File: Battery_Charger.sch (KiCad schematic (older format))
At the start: 40 parts, among them J1 OpenVent_Barrel_Connector, Q10 2N7002BK, Q11 2N7002BK, Q12 2N7002BK, Q8 PBSS5350Z, U13 TLV7042DGKR, U14 BQ24450DW, U16 TLV2333IDR

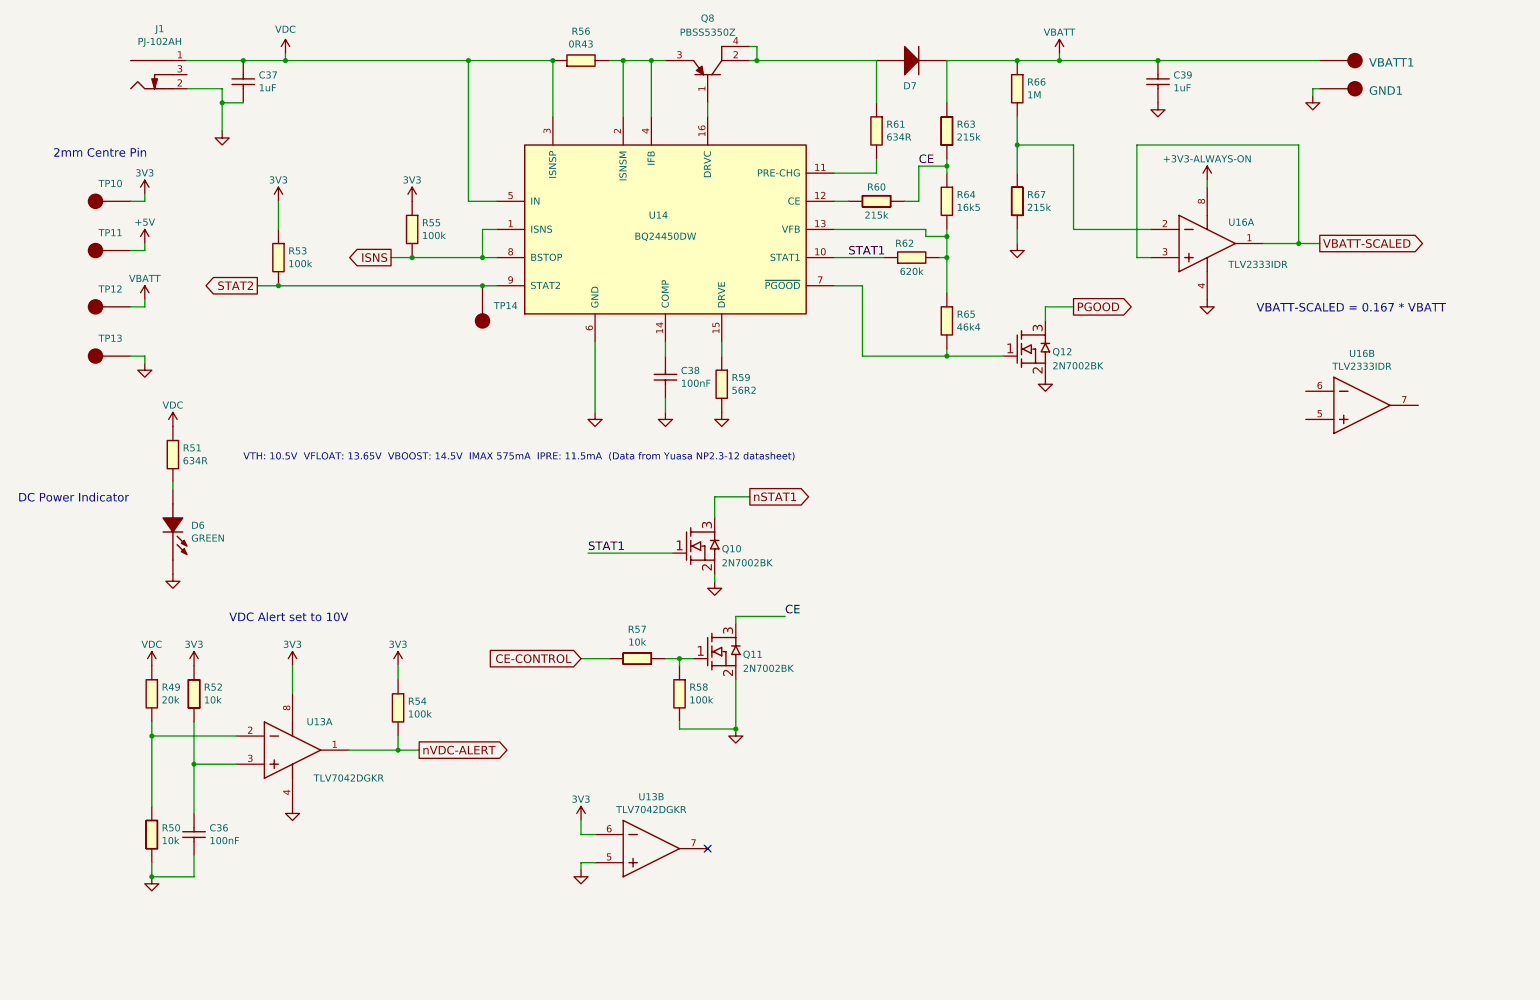
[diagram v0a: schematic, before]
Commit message: Still had some text cleanups to do plus fixed a couple of minor circuit issues.
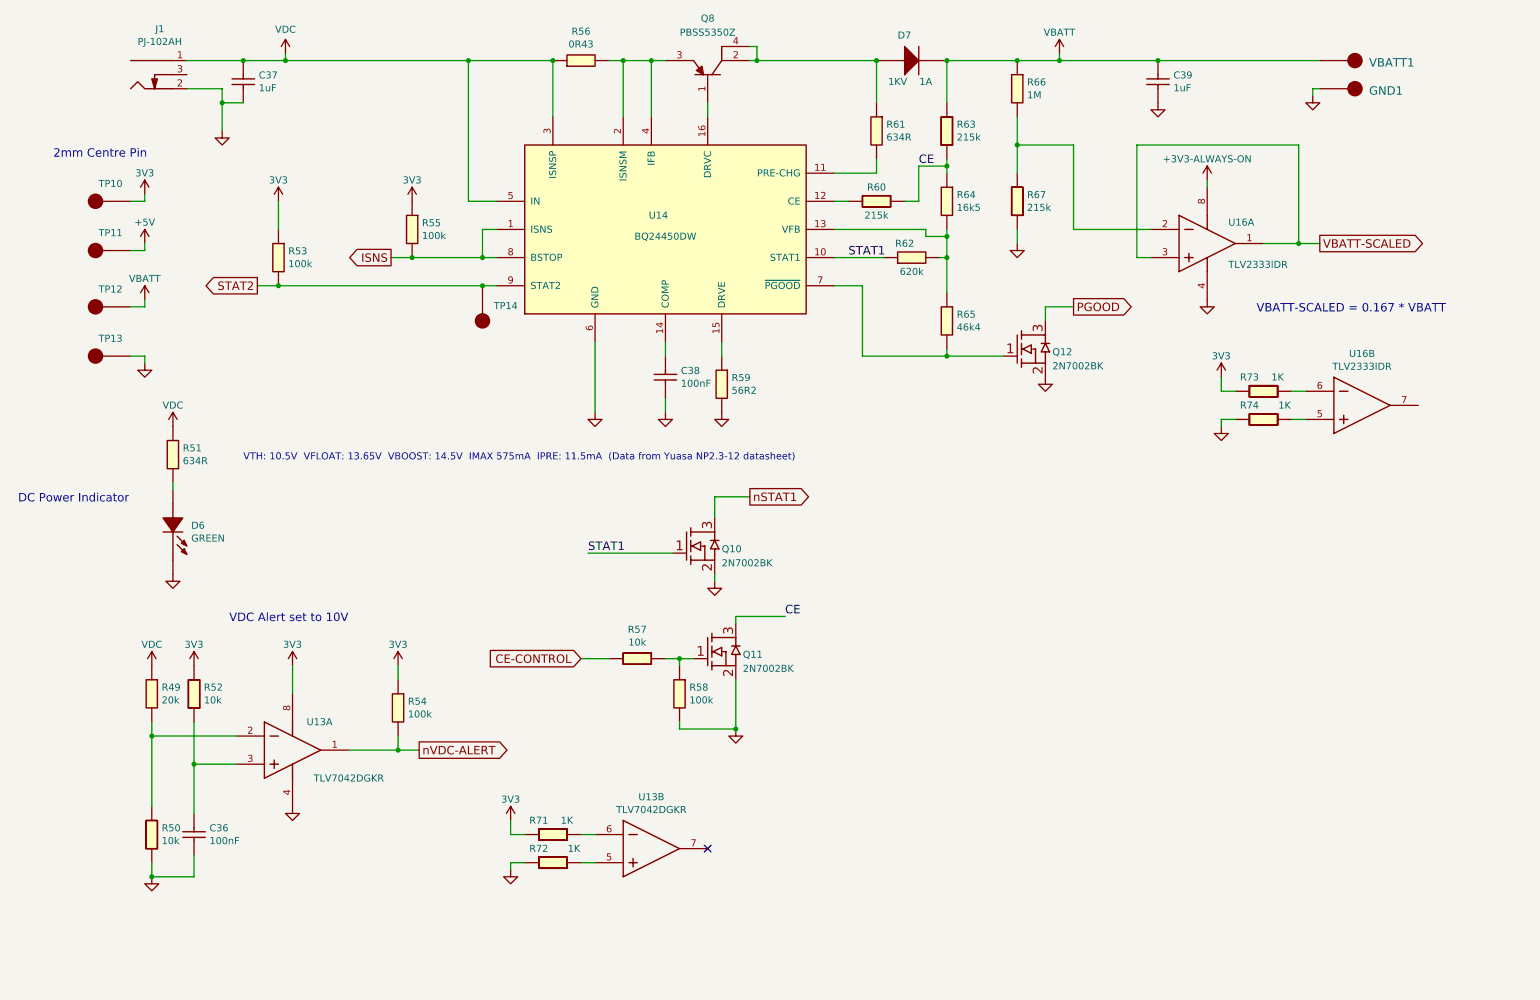
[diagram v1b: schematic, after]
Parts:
- added R71, R72, R73, R74: 1K_0603_Chip_Resistor,_1%,_0.1W, symbol OpenVent:1K_0603_Chip_Resistor,_1%,_0.1W
- D7: value ~ -> DIODE_GEN_PURP_1KV_1A_SMA; Current (none) -> 1A; ManufacturerPN S1M-13-F -> (none); Mfr_PN (none) -> S1M-13-F; Voltage (none) -> 1KV
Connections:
- net +3V3: now also R71.1, R73.1; no longer U13.6 (INB-)
- net GND: now also R72.1, R74.1; no longer U13.5 (INB+)
- net at U16.5 (INB+): now also R74.2
- net at U16.6 (INB-): now also R73.2
- new net: R71.2, U13.6 (INB-)
- new net: R72.2, U13.5 (INB+)
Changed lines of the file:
@@
 L OpenVent:GND #GND_047
 U 1 1 5F8DD1BD
-P 4550 6800
-F 0 "#GND_047" H 4550 6800 20  0001 C CNN
-F 1 "GND" H 4550 6730 30  0001 C CNN
-F 2 "" H 4550 6800 70  0000 C CNN
-F 3 "" H 4550 6800 70  0000 C CNN
-	1    4550 6800
+P 4050 6800
+F 0 "#GND_047" H 4050 6800 20  0001 C CNN
+F 1 "GND" H 4050 6730 30  0001 C CNN
+F 2 "" H 4050 6800 70  0000 C CNN
+F 3 "" H 4050 6800 70  0000 C CNN
+	1    4050 6800
 	1    0    0    -1
 $EndComp
@@
 L OpenVent:3V3 #3V3_015
 U 1 1 5F8DD1B6
-P 4550 6450
-F 0 "#3V3_015" H 4550 6450 20  0001 C CNN
-F 1 "3V3" H 4550 6600 50  0000 C CNN
-F 2 "" H 4550 6450 70  0000 C CNN
-F 3 "" H 4550 6450 70  0000 C CNN
-	1    4550 6450
+P 4050 6450
+F 0 "#3V3_015" H 4050 6450 20  0001 C CNN
+F 1 "3V3" H 4050 6600 50  0000 C CNN
+F 2 "" H 4050 6450 70  0000 C CNN
+F 3 "" H 4050 6450 70  0000 C CNN
+	1    4050 6450
 	1    0    0    -1
 $EndComp
@@
 U 1 1 5F8DD18B
 P 6900 1050
-F 0 "D7" H 6840 840 50  0000 L BNN
-F 1 "~" H 6900 1050 50  0001 C CNN
+F 0 "D7" H 6800 1200 50  0000 L BNN
+F 1 "DIODE_GEN_PURP_1KV_1A_SMA" H 6900 1050 50  0001 C CNN
 F 2 "" H 6900 1050 50  0001 C CNN
 F 3 "" H 6900 1050 50  0001 C CNN
-F 4 "S1M-13-F" V 1200 -1550 50  0001 C CNN "ManufacturerPN"
+F 4 "S1M-13-F" V 1200 -1550 50  0001 C CNN "Mfr_PN"
+F 5 "1A" H 7000 900 50  0000 C CNN "Current"
+F 6 "1KV" H 6800 900 50  0000 C CNN "Voltage"
 	1    6900 1050
 	1    0    0    -1
@@
 Wire Wire Line
 	9000 1950 9000 1900
-Wire Wire Line
-	4650 6550 4550 6550
-Wire Wire Line
-	4550 6550 4550 6450
-Wire Wire Line
-	4650 6750 4550 6750
-Wire Wire Line
-	4550 6750 4550 6800
 Wire Wire Line
 	5500 4750 5500 4700
@@
 	0    1    1    0
 $EndComp
+Connection ~ 6650 1050
+Connection ~ 7150 1050
+$Comp
+L OpenVent:1K_0603_Chip_Resistor,_1%,_0.1W R71
+U 1 1 5F99EF98
+P 4250 6450
+F 0 "R71" H 4250 6450 50  0000 C CNN
+F 1 "1K_0603_Chip_Resistor,_1%,_0.1W" H 4250 6450 50  0001 C CNN
+F 2 "" H 4250 6450 60  0001 C CNN
+F 3 "" H 4250 6450 60  0001 C CNN
+F 4 "1K" H 4450 6450 50  0000 C CNN "Val"
+F 5 "1%" H 4350 6465 50  0001 C CNN "Tolerance"
+	1    4250 6450
+	1    0    0    -1
+$EndComp
+$Comp
+L OpenVent:1K_0603_Chip_Resistor,_1%,_0.1W R72
+U 1 1 5F99FB5D
+P 4250 6650
+F 0 "R72" H 4250 6650 50  0000 C CNN
+F 1 "1K_0603_Chip_Resistor,_1%,_0.1W" H 4250 6650 50  0001 C CNN
+F 2 "" H 4250 6650 60  0001 C CNN
+F 3 "" H 4250 6650 60  0001 C CNN
+F 4 "1K" H 4500 6650 50  0000 C CNN "Val"
+F 5 "1%" H 4350 6665 50  0001 C CNN "Tolerance"
+	1    4250 6650
+	1    0    0    -1
+$EndComp
+$Comp
+L OpenVent:GND #GND_058
+U 1 1 5F9A873A
+P 9100 3650
+F 0 "#GND_058" H 9100 3650 20  0001 C CNN
+F 1 "GND" H 9100 3580 30  0001 C CNN
+F 2 "" H 9100 3650 70  0000 C CNN
+F 3 "" H 9100 3650 70  0000 C CNN
+	1    9100 3650
+	1    0    0    -1
+$EndComp
+$Comp
+L OpenVent:3V3 #3V3_016
+U 1 1 5F9A8740
+P 9100 3300
+F 0 "#3V3_016" H 9100 3300 20  0001 C CNN
+F 1 "3V3" H 9100 3450 50  0000 C CNN
+F 2 "" H 9100 3300 70  0000 C CNN
+F 3 "" H 9100 3300 70  0000 C CNN
+	1    9100 3300
+	1    0    0    -1
+$EndComp
+$Comp
+L OpenVent:1K_0603_Chip_Resistor,_1%,_0.1W R73
+U 1 1 5F9A8748
+P 9300 3300
+F 0 "R73" H 9300 3300 50  0000 C CNN
+F 1 "1K_0603_Chip_Resistor,_1%,_0.1W" H 9300 3300 50  0001 C CNN
+F 2 "" H 9300 3300 60  0001 C CNN
+F 3 "" H 9300 3300 60  0001 C CNN
+F 4 "1K" H 9500 3300 50  0000 C CNN "Val"
+F 5 "1%" H 9400 3315 50  0001 C CNN "Tolerance"
+	1    9300 3300
+	1    0    0    -1
+$EndComp
+$Comp
+L OpenVent:1K_0603_Chip_Resistor,_1%,_0.1W R74
+U 1 1 5F9A8750
+P 9300 3500
+F 0 "R74" H 9300 3500 50  0000 C CNN
+F 1 "1K_0603_Chip_Resistor,_1%,_0.1W" H 9300 3500 50  0001 C CNN
+F 2 "" H 9300 3500 60  0001 C CNN
+F 3 "" H 9300 3500 60  0001 C CNN
+F 4 "1K" H 9550 3500 50  0000 C CNN "Val"
+F 5 "1%" H 9400 3515 50  0001 C CNN "Tolerance"
+	1    9300 3500
+	1    0    0    -1
+$EndComp
+Wire Wire Line
+	9700 3400 9600 3400
+Wire Wire Line
+	9200 3400 9100 3400
+Wire Wire Line
+	9100 3300 9100 3400
+Wire Wire Line
+	9200 3600 9100 3600
+Wire Wire Line
+	9100 3600 9100 3650
+Wire Wire Line
+	9700 3600 9600 3600
+Wire Wire Line
+	4650 6550 4550 6550
+Wire Wire Line
+	4150 6550 4050 6550
+Wire Wire Line
+	4050 6550 4050 6450
+Wire Wire Line
+	4650 6750 4550 6750
+Wire Wire Line
+	4150 6750 4050 6750
+Wire Wire Line
+	4050 6750 4050 6800
 $EndSCHEMATC

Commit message: Updating my local branch, wip Friday 10/30/20.  Got sucked into fixing up the libraries for the BOM...
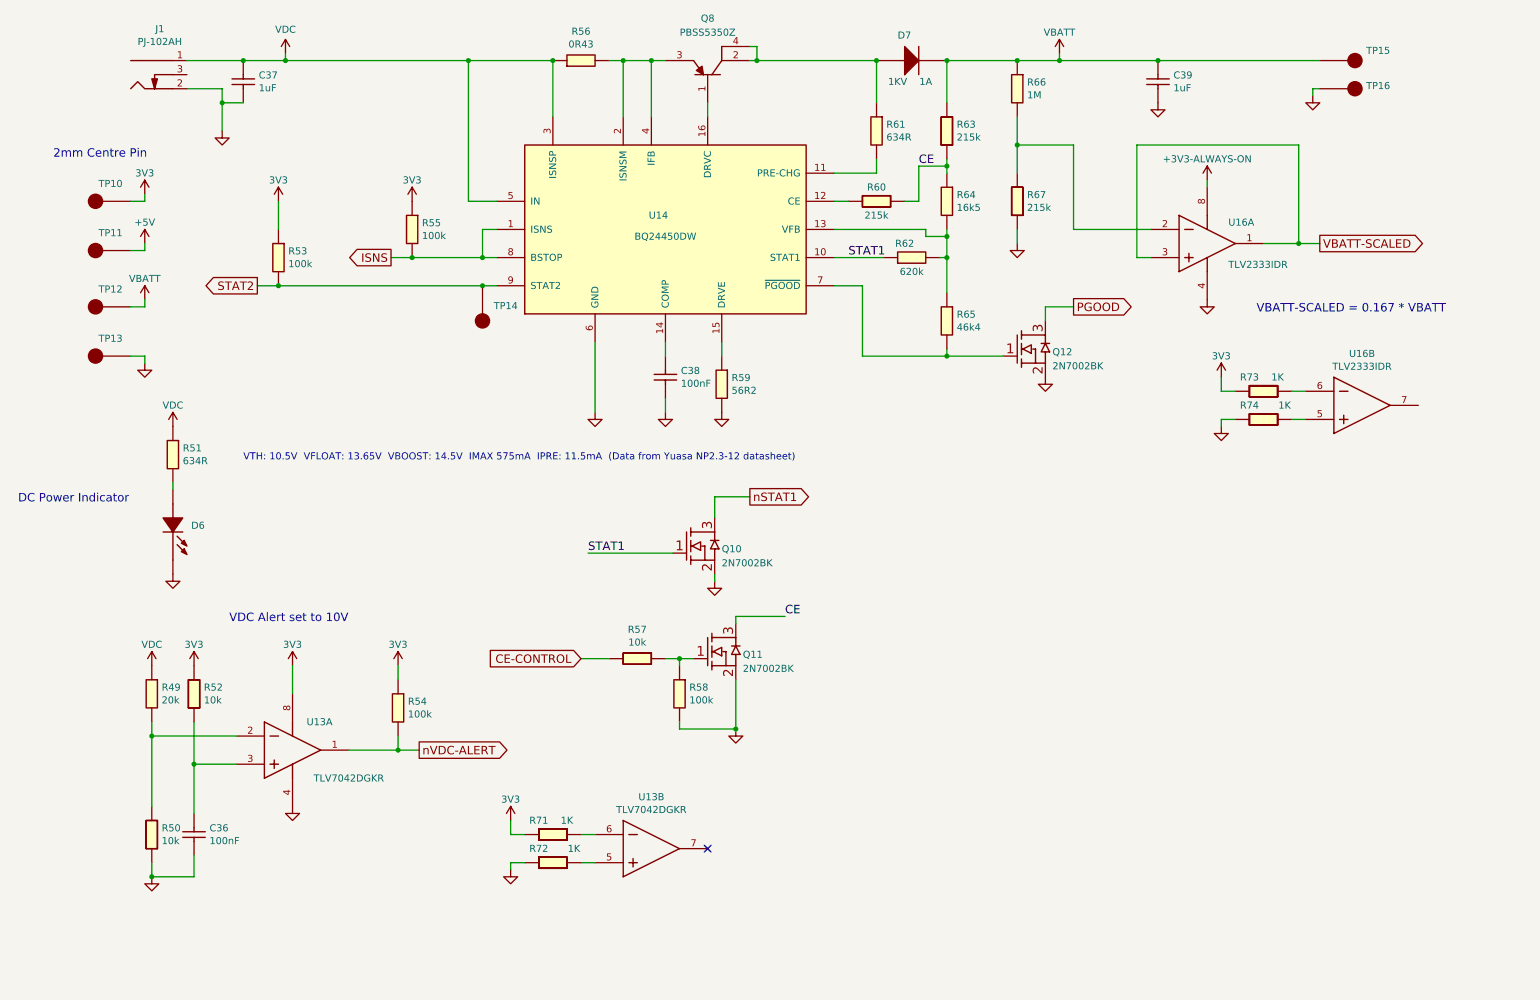
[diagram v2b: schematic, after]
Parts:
- C36, C37, C38, C39: footprint (none) -> Capacitor_SMD:C_0603_1608Metric
- D6: footprint (none) -> LED_SMD:LED_0603_1608Metric; Colour (none) -> GREEN; Val GREEN -> (none)
- D7: footprint (none) -> Diode_SMD:D_SMA; Desc (none) -> DIODE GEN PURP 1KV 1A SMA; DistName (none) -> DigiKey; Dist_PN (none) -> S1M-FDITR-ND; Mfr (none) -> Diodes Incorporated
- J1: footprint (none) -> Connector_BarrelJack:BarrelJack_CUI_PJ-102AH_Horizontal
- Q10, Q11, Q12: footprint (none) -> Package_TO_SOT_SMD:SOT-23
- Q8: footprint (none) -> Package_TO_SOT_SMD:SOT-223; Current (none) -> 3A; Desc (none) -> TRANS PNP 50V 3A SOT223; Detailed (none) -> Bipolar (BJT) Transistor PNP 100MHz Surface Mount SOT-223; DistName (none) -> DigiKey; Dist_PN (none) -> 1727-3914-2-ND; Mfr (none) -> Nexperia USA Inc.; Voltage (none) -> 50V
- R49, R50, R51, R52, R53, R54, R55, R57, R58, R59, R60, R61, R62, R63, R64, R65, R66, R67, R71, R72, R73, R74: footprint (none) -> Resistor_SMD:R_0603_1608Metric
- R56: footprint (none) -> Resistor_SMD:R_1210_3225Metric
- TP10, TP11, TP12, TP13, TP14: footprint (none) -> TestPoint:TestPoint_Pad_2.0x2.0mm
- TP15: renamed from VBATT1; value ~ -> Test_Point_PTH; footprint (none) -> TestPoint:TestPoint_Pad_2.0x2.0mm
- TP16: renamed from GND1; value ~ -> Test_Point_PTH; footprint (none) -> TestPoint:TestPoint_Pad_2.0x2.0mm
